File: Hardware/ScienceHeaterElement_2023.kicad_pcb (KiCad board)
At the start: 2 copper layers, 82.4 x 33.6 mm, 12 parts, among them Q1 BUK7M6R3-40EX, U1 LMT85DCK

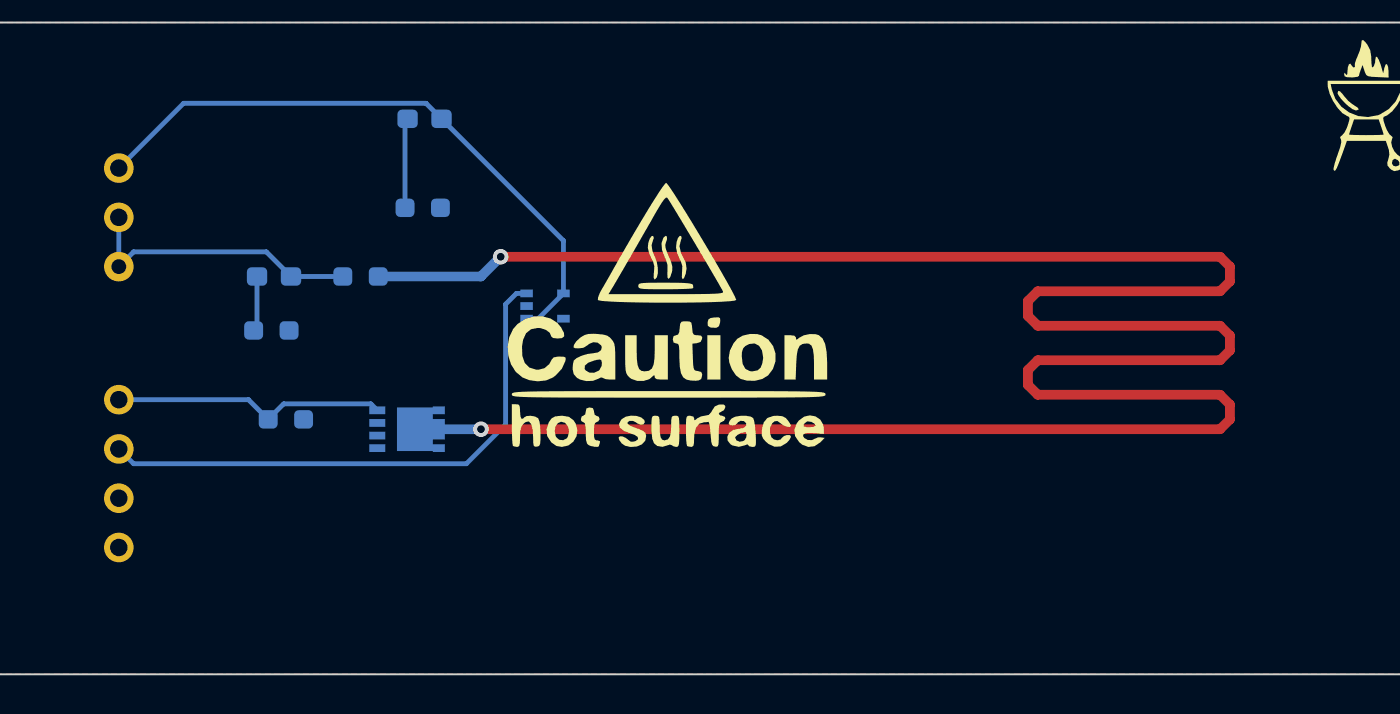
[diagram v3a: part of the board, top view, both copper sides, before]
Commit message: Edited heater traces and blockout area
Increased the blockout area to a .75 by .75 and edited the heater traces to fit the new area. Added text to label the board. Moved temp sensor closer to the heater traces.
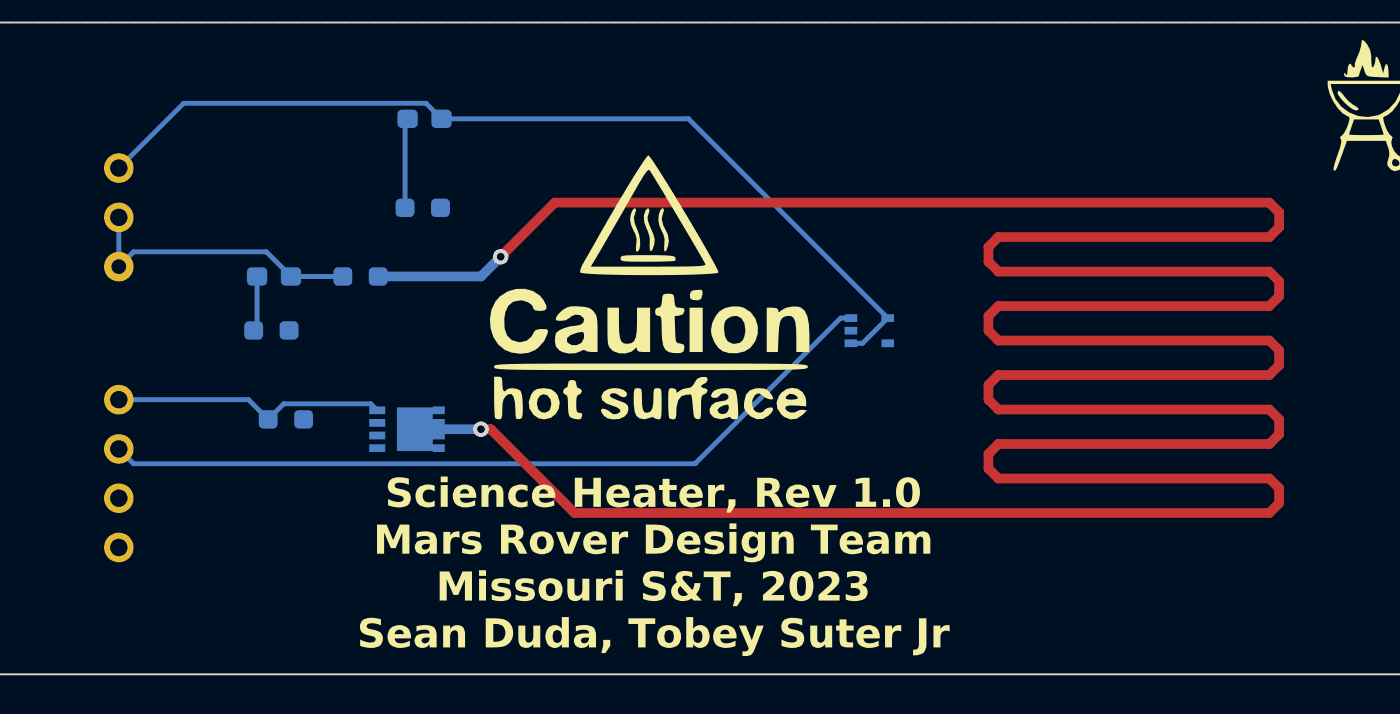
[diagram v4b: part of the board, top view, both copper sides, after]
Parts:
- moved U1 16.8 mm to (122.9, 53.1)
- moved G*** 1.69 mm to (111.5, 50.8)
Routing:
- net /Heater_Trace: track 134.0 -> 225.0 mm
- net +3.3V: track 32.4 -> 48.0 mm
- net Temp_Sense: track 28.6 -> 41.2 mm
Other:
- board text added: "Science Heater, Rev 1.0 Mars Rover Design Team Missouri S&T, 2023 Sean Duda, Tobey Suter Jr"
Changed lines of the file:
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@@
   )
   (footprint "LOGO" (layer "F.Cu")
-    (at 112.42 52.22)
+    (at 111.506 50.8)
     (attr board_only exclude_from_pos_files exclude_from_bom)
     (fp_text reference "G***" (at 5.51 -11.48) (layer "F.SilkS") hide
@@
         (effects (font (size 1 1) (thickness 0.15)) (justify mirror))
     )
-    (fp_text value "BUK7M6R3-40EX" (at 0.155 -3.1) (layer "B.Fab")
+    (fp_text value "BUK7M6R3-40EX" (at 1.013 -2.734) (layer "B.Fab")
         (effects (font (size 1 1) (thickness 0.15)) (justify mirror))
     )
@@
   )
   (footprint "Package_TO_SOT_SMD:SOT-353_SC-70-5" (layer "B.Cu")
-    (at 106.172 51.816)
+    (at 122.89 53.086)
     (descr "SOT-353, SC-70-5")
     (tags "SOT-353 SC-70-5")
@@
   (gr_arc (start 153.4 69.4) (mid 152.989949 70.389949) (end 152 70.8)
     (stroke (width 0.1) (type default)) (layer "Edge.Cuts"))
+  (gr_text "Science Heater, Rev 1.0\nMars Rover Design Team\nMissouri S&T, 2023\nSean Duda, Tobey Suter Jr" (at 111.76 69.596) (layer "F.SilkS")
+    (effects (font (size 1.5 1.5) (thickness 0.3) bold) (justify bottom))
+  )
   (segment (start 84.201 44.704) (end 87.541 41.364) (width 0.25) (layer "B.Cu") (net 1))
+  (segment (start 123.84 52.436) (end 113.568 42.164) (width 0.25) (layer "B.Cu") (net 1))
   (segment (start 100.038 41.364) (end 100.838 42.164) (width 0.25) (layer "B.Cu") (net 1))
-  (segment (start 107.122 51.166) (end 107.122 48.448) (width 0.25) (layer "B.Cu") (net 1))
-  (segment (start 105.222 52.466) (end 105.822 52.466) (width 0.25) (layer "B.Cu") (net 1))
+  (segment (start 121.94 53.736) (end 122.54 53.736) (width 0.25) (layer "B.Cu") (net 1))
   (segment (start 87.541 41.364) (end 100.038 41.364) (width 0.25) (layer "B.Cu") (net 1))
-  (segment (start 107.122 48.448) (end 100.838 42.164) (width 0.25) (layer "B.Cu") (net 1))
-  (segment (start 105.822 52.466) (end 107.122 51.166) (width 0.25) (layer "B.Cu") (net 1))
+  (segment (start 113.568 42.164) (end 100.838 42.164) (width 0.25) (layer "B.Cu") (net 1))
+  (segment (start 122.54 53.736) (end 123.84 52.436) (width 0.25) (layer "B.Cu") (net 1))
   (segment (start 92.964 53.086) (end 92.9765 53.0735) (width 0.254) (layer "B.Cu") (net 2))
   (segment (start 84.201 49.784) (end 84.201 47.244) (width 0.25) (layer "B.Cu") (net 3))
@@
   (segment (start 97.525 57.191) (end 97.192 56.858) (width 0.25) (layer "B.Cu") (net 6))
   (segment (start 97.192 56.858) (end 92.701 56.858) (width 0.25) (layer "B.Cu") (net 6))
-  (segment (start 131.064 52.324) (end 131.064 51.562) (width 0.5) (layer "F.Cu") (net 7))
-  (segment (start 140.97 49.276) (end 103.886 49.276) (width 0.5) (layer "F.Cu") (net 7))
-  (segment (start 131.064 51.562) (end 131.572 51.054) (width 0.5) (layer "F.Cu") (net 7))
-  (segment (start 141.478 57.658) (end 141.478 56.896) (width 0.5) (layer "F.Cu") (net 7))
-  (segment (start 140.97 51.054) (end 141.478 50.546) (width 0.5) (layer "F.Cu") (net 7))
-  (segment (start 141.478 53.34) (end 140.97 52.832) (width 0.5) (layer "F.Cu") (net 7))
-  (segment (start 141.478 54.102) (end 141.478 53.34) (width 0.5) (layer "F.Cu") (net 7))
-  (segment (start 140.97 56.388) (end 131.572 56.388) (width 0.5) (layer "F.Cu") (net 7))
-  (segment (start 141.478 50.546) (end 141.478 49.784) (width 0.5) (layer "F.Cu") (net 7))
-  (segment (start 131.572 54.61) (end 140.97 54.61) (width 0.5) (layer "F.Cu") (net 7))
-  (segment (start 140.97 54.61) (end 141.478 54.102) (width 0.5) (layer "F.Cu") (net 7))
-  (segment (start 141.478 56.896) (end 140.97 56.388) (width 0.5) (layer "F.Cu") (net 7))
-  (segment (start 131.064 55.88) (end 131.064 55.118) (width 0.5) (layer "F.Cu") (net 7))
-  (segment (start 141.478 49.784) (end 140.97 49.276) (width 0.5) (layer "F.Cu") (net 7))
-  (segment (start 140.97 58.166) (end 141.478 57.658) (width 0.5) (layer "F.Cu") (net 7))
-  (segment (start 131.572 51.054) (end 140.97 51.054) (width 0.5) (layer "F.Cu") (net 7))
-  (segment (start 131.572 56.388) (end 131.064 55.88) (width 0.5) (layer "F.Cu") (net 7))
-  (segment (start 102.87 58.166) (end 140.97 58.166) (width 0.5) (layer "F.Cu") (net 7))
-  (segment (start 131.572 52.832) (end 131.064 52.324) (width 0.5) (layer "F.Cu") (net 7))
-  (segment (start 131.064 55.118) (end 131.572 54.61) (width 0.5) (layer "F.Cu") (net 7))
-  (segment (start 140.97 52.832) (end 131.572 52.832) (width 0.5) (layer "F.Cu") (net 7))
+  (segment (start 129.54 50.038) (end 143.51 50.038) (width 0.5) (layer "F.Cu") (net 7))
+  (segment (start 143.51 53.594) (end 144.018 54.102) (width 0.5) (layer "F.Cu") (net 7))
+  (segment (start 143.51 57.15) (end 144.018 57.658) (width 0.5) (layer "F.Cu") (net 7))
+  (segment (start 144.018 51.308) (end 143.51 51.816) (width 0.5) (layer "F.Cu") (net 7))
+  (segment (start 129.032 55.88) (end 129.032 56.642) (width 0.5) (layer "F.Cu") (net 7))
+  (segment (start 103.886 49.276) (end 106.68 46.482) (width 0.5) (layer "F.Cu") (net 7))
+  (segment (start 129.54 57.15) (end 143.51 57.15) (width 0.5) (layer "F.Cu") (net 7))
+  (segment (start 106.68 46.482) (end 143.51 46.482) (width 0.5) (layer "F.Cu") (net 7))
+  (segment (start 143.51 60.706) (end 144.018 61.214) (width 0.5) (layer "F.Cu") (net 7))
+  (segment (start 129.032 48.768) (end 129.032 49.53) (width 0.5) (layer "F.Cu") (net 7))
+  (segment (start 144.018 61.214) (end 144.018 61.976) (width 0.5) (layer "F.Cu") (net 7))
+  (segment (start 103.378 58.166) (end 102.87 58.166) (width 0.5) (layer "F.Cu") (net 7))
+  (segment (start 129.032 49.53) (end 129.54 50.038) (width 0.5) (layer "F.Cu") (net 7))
+  (segment (start 144.018 50.546) (end 144.018 51.308) (width 0.5) (layer "F.Cu") (net 7))
+  (segment (start 143.51 46.482) (end 144.018 46.99) (width 0.5) (layer "F.Cu") (net 7))
+  (segment (start 129.032 53.086) (end 129.54 53.594) (width 0.5) (layer "F.Cu") (net 7))
+  (segment (start 129.54 51.816) (end 129.032 52.324) (width 0.5) (layer "F.Cu") (net 7))
+  (segment (start 144.018 61.976) (end 143.51 62.484) (width 0.5) (layer "F.Cu") (net 7))
+  (segment (start 144.018 58.42) (end 143.51 58.928) (width 0.5) (layer "F.Cu") (net 7))
+  (segment (start 144.018 46.99) (end 144.018 47.752) (width 0.5) (layer "F.Cu") (net 7))
+  (segment (start 129.54 60.706) (end 143.51 60.706) (width 0.5) (layer "F.Cu") (net 7))
+  (segment (start 129.54 55.372) (end 129.032 55.88) (width 0.5) (layer "F.Cu") (net 7))
+  (segment (start 129.54 53.594) (end 143.51 53.594) (width 0.5) (layer "F.Cu") (net 7))
+  (segment (start 143.51 55.372) (end 129.54 55.372) (width 0.5) (layer "F.Cu") (net 7))
+  (segment (start 144.018 54.102) (end 144.018 54.864) (width 0.5) (layer "F.Cu") (net 7))
+  (segment (start 143.51 58.928) (end 129.54 58.928) (width 0.5) (layer "F.Cu") (net 7))
+  (segment (start 129.032 60.198) (end 129.54 60.706) (width 0.5) (layer "F.Cu") (net 7))
+  (segment (start 144.018 47.752) (end 143.51 48.26) (width 0.5) (layer "F.Cu") (net 7))
+  (segment (start 143.51 48.26) (end 129.54 48.26) (width 0.5) (layer "F.Cu") (net 7))
+  (segment (start 107.696 62.484) (end 103.378 58.166) (width 0.5) (layer "F.Cu") (net 7))
+  (segment (start 143.51 50.038) (end 144.018 50.546) (width 0.5) (layer "F.Cu") (net 7))
+  (segment (start 129.54 48.26) (end 129.032 48.768) (width 0.5) (layer "F.Cu") (net 7))
+  (segment (start 129.54 58.928) (end 129.032 59.436) (width 0.5) (layer "F.Cu") (net 7))
+  (segment (start 143.51 51.816) (end 129.54 51.816) (width 0.5) (layer "F.Cu") (net 7))
+  (segment (start 129.032 56.642) (end 129.54 57.15) (width 0.5) (layer "F.Cu") (net 7))
+  (segment (start 143.51 62.484) (end 107.696 62.484) (width 0.5) (layer "F.Cu") (net 7))
+  (segment (start 144.018 57.658) (end 144.018 58.42) (width 0.5) (layer "F.Cu") (net 7))
+  (segment (start 129.032 59.436) (end 129.032 60.198) (width 0.5) (layer "F.Cu") (net 7))
+  (segment (start 144.018 54.864) (end 143.51 55.372) (width 0.5) (layer "F.Cu") (net 7))
+  (segment (start 129.032 52.324) (end 129.032 53.086) (width 0.5) (layer "F.Cu") (net 7))
   (via (at 102.87 58.166) (size 0.8) (drill 0.4) (layers "F.Cu" "B.Cu") (net 7))
   (via (at 103.886 49.276) (size 0.8) (drill 0.4) (layers "F.Cu" "B.Cu") (net 7))
@@
   (segment (start 99.555 58.256) (end 99.465 58.166) (width 0.5) (layer "B.Cu") (net 7))
   (segment (start 102.87 50.292) (end 97.5735 50.292) (width 0.5) (layer "B.Cu") (net 7))
-  (segment (start 104.14 57.921305) (end 102.117305 59.944) (width 0.25) (layer "B.Cu") (net 8))
-  (segment (start 104.697 51.166) (end 104.14 51.723) (width 0.25) (layer "B.Cu") (net 8))
-  (segment (start 84.201 59.182) (end 84.963 59.944) (width 0.25) (layer "B.Cu") (net 8))
-  (segment (start 105.222 51.166) (end 104.697 51.166) (width 0.25) (layer "B.Cu") (net 8))
-  (segment (start 104.14 51.723) (end 104.14 57.921305) (width 0.25) (layer "B.Cu") (net 8))
-  (segment (start 84.963 59.944) (end 102.117305 59.944) (width 0.25) (layer "B.Cu") (net 8))
+  (segment (start 84.963 59.944) (end 84.201 59.182) (width 0.25) (layer "B.Cu") (net 8))
+  (segment (start 121.415 52.436) (end 113.907 59.944) (width 0.25) (layer "B.Cu") (net 8))
+  (segment (start 113.907 59.944) (end 84.963 59.944) (width 0.25) (layer "B.Cu") (net 8))
+  (segment (start 121.94 52.436) (end 121.415 52.436) (width 0.25) (layer "B.Cu") (net 8))
   (zone (net 2) (net_name "GND") (layer "F.Cu") (hatch edge 0.5)
     (priority 1)
@@
     (polygon
       (pts
-        (xy 129.794 46.99)
-        (xy 142.748 46.99)
-        (xy 142.758 66.29)
-        (xy 129.804 66.29)
-      )
-    )
+        (xy 126.996799 44.708)
+        (xy 146.046799 44.708)
+        (xy 146.056799 63.754)
+        (xy 127.006799 63.754)
+      )
+    )

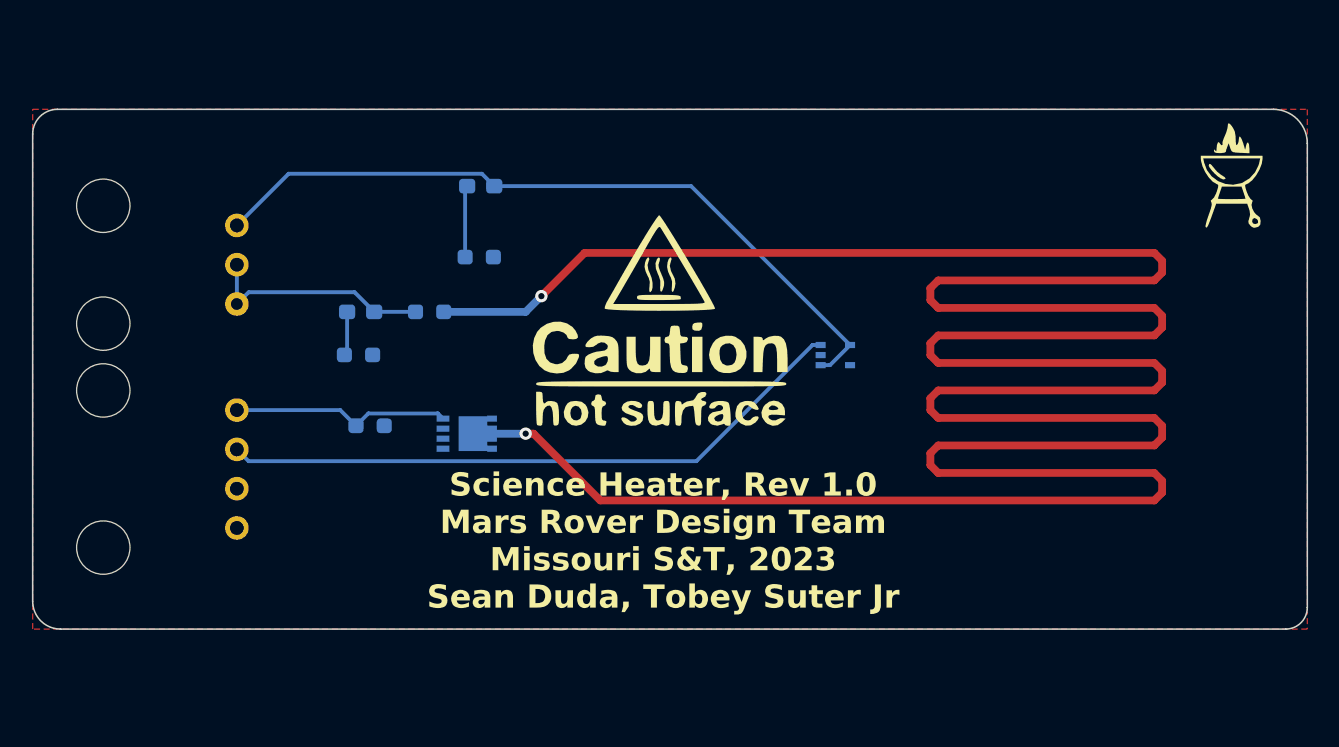
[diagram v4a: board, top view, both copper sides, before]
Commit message: Changed overall size and heating trace area
Changed size and heating trace area to more effectively heat the microfluidic chips
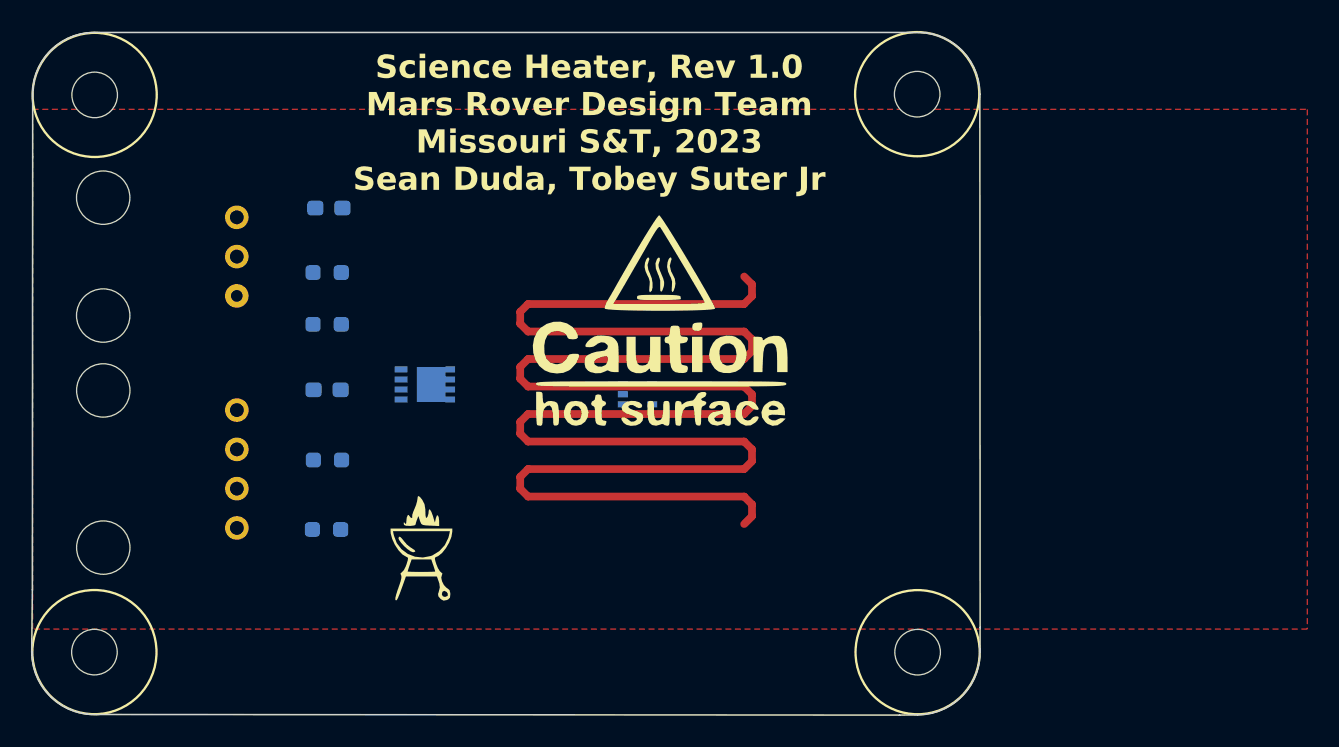
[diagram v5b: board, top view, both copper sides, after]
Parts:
- added REF**: 4_40_Hole, MRDT_Drill_Holes:4_40_Hole_Corner, F.Cu at (79.0, 68.3)
- added REF**: 4_40_Hole, MRDT_Drill_Holes:4_40_Hole_Corner, F.Cu at (79.0, 40.3)
- added REF**: 4_40_Hole, MRDT_Drill_Holes:4_40_Hole_Corner, F.Cu at (124.2, 68.3)
- added REF**: 4_40_Hole, MRDT_Drill_Holes:4_40_Hole_Corner, F.Cu at (124.2, 40.2)
- moved G*** 57.7 mm to (96.1, 65.3)
- moved U1 13.0 mm to (110.1, 55.6)
- moved D1 9.92 mm to (90.1, 43.6)
- moved R2 9.88 mm to (90.0, 47.8)
- moved R4 7.27 mm to (90.0, 64.4)
- moved R3 7.09 mm to (90.1, 59.9)
- moved R1 6.67 mm to (90.0, 51.1)
- moved D2 5.48 mm to (90.0, 55.3)
- moved Q1 4.18 mm to (96.4, 55.0)
- moved Conn1 0.52 mm to (84.2, 44.2)
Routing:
- net /Heater_Trace: track 225.0 -> 131.5 mm, vias 2 -> 0
- net +3.3V: track 48.0 -> 0.00 mm
- net Temp_Sense: track 41.2 -> 0.00 mm
- net +12V: track 14.9 -> 0.00 mm
- net Gate_Driving_Pin: track 14.2 -> 0.00 mm
- net Net-(D1-K): track 4.64 -> 0.00 mm
- net Net-(D2-K): track 3.18 -> 0.00 mm
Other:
- board size 82.4 x 33.6 mm -> 61.3 x 44.1 mm
